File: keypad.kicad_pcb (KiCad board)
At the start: 2 copper layers, 10 parts, among them SW1 SW_Push, SW2 SW_Push, SW3 SW_Push, SW4 SW_Push, SW5 SW_Push, SW6 SW_Push, SW7 SW_Push, SW8 SW_Push, SW9 SW_Push, U1 ESP32-S3-DevKitC-1

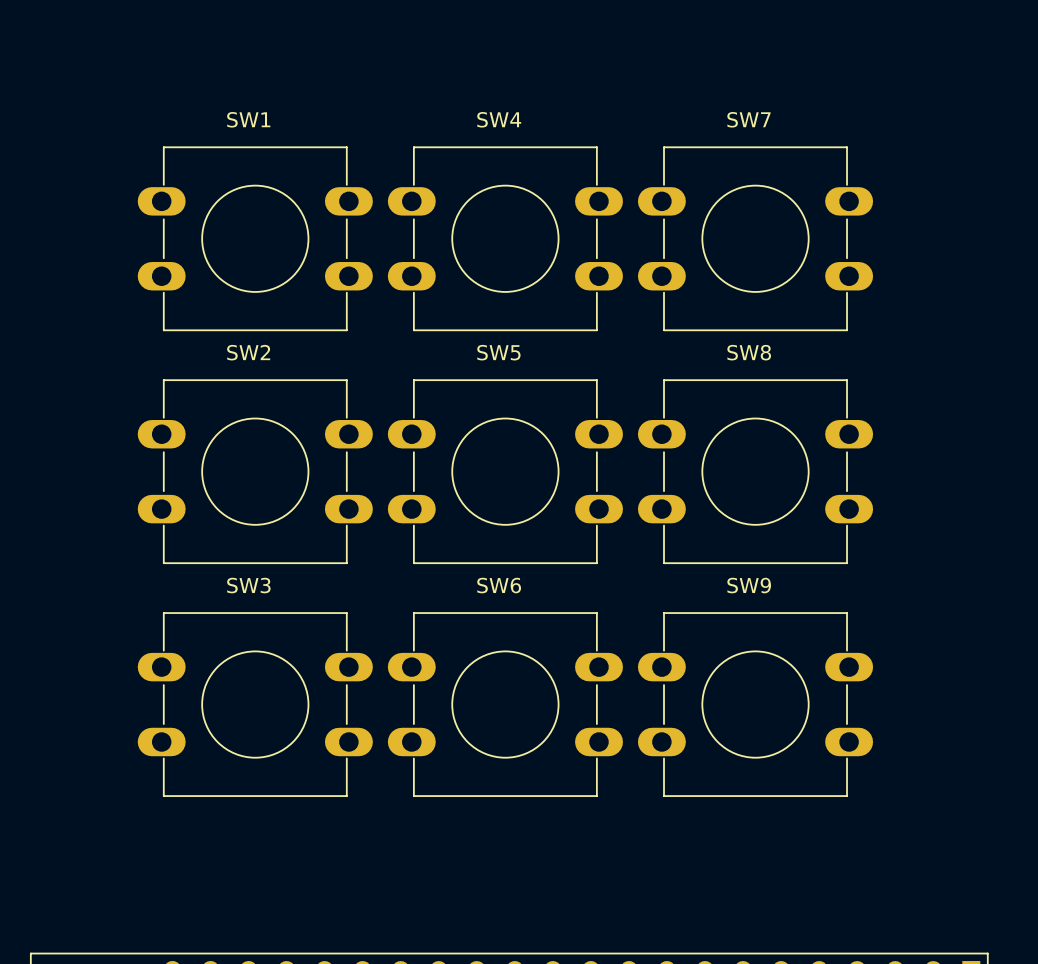
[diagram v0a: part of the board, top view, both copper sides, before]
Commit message: spaced out buttons
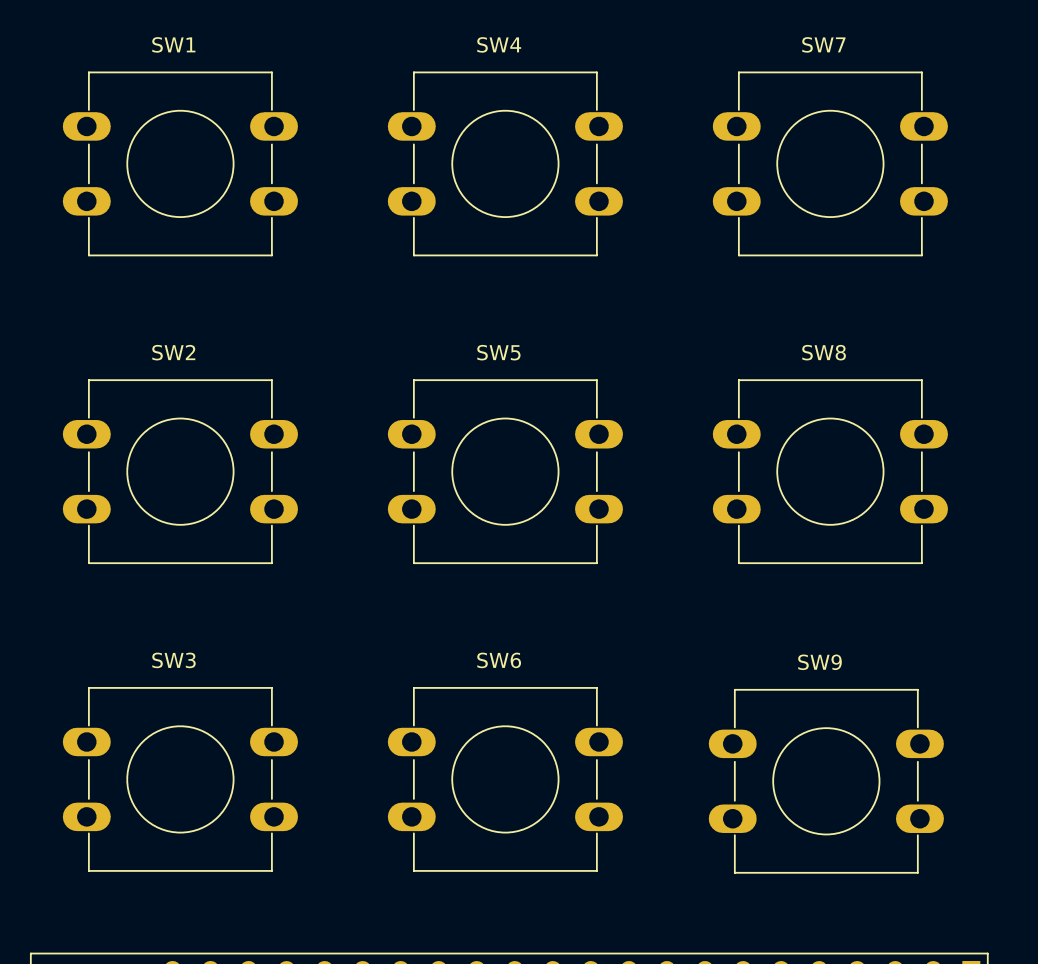
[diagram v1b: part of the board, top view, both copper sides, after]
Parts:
- moved SW1 7.07 mm to (123.6, 66.3)
- moved SW3 7.07 mm to (123.6, 107.4)
- moved SW7 7.07 mm to (167.0, 66.3)
- moved SW9 6.97 mm to (166.8, 107.5)
- moved SW2 5.00 mm to (123.6, 86.8)
- moved SW4 5.00 mm to (145.3, 66.3)
- moved SW6 5.00 mm to (145.3, 107.4)
- moved SW8 5.00 mm to (167.0, 86.8)
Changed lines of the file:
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@@
 	(footprint "Button_Switch_THT:SW_PUSH-12mm"
 		(layer "F.Cu")
-		(at 145.32 102.375)
+		(at 145.32 107.375)
 		(descr "Generic SW PUSH 12mm, e.g https://sten-eswitch-13110800-production.s3.amazonaws.com/system/asset/product_line/data_sheet/143/TL1100.pdf")
 		(tags "tact sw push 12mm")
@@
 	(footprint "Button_Switch_THT:SW_PUSH-12mm"
 		(layer "F.Cu")
-		(at 162.02 71.275)
+		(at 167.02 66.275)
 		(descr "Generic SW PUSH 12mm, e.g https://sten-eswitch-13110800-production.s3.amazonaws.com/system/asset/product_line/data_sheet/143/TL1100.pdf")
 		(tags "tact sw push 12mm")
@@
 	(footprint "Button_Switch_THT:SW_PUSH-12mm"
 		(layer "F.Cu")
-		(at 128.62 86.825)
+		(at 123.62 86.825)
 		(descr "Generic SW PUSH 12mm, e.g https://sten-eswitch-13110800-production.s3.amazonaws.com/system/asset/product_line/data_sheet/143/TL1100.pdf")
 		(tags "tact sw push 12mm")
@@
 	(footprint "Button_Switch_THT:SW_PUSH-12mm"
 		(layer "F.Cu")
-		(at 128.62 71.275)
+		(at 123.62 66.275)
 		(descr "Generic SW PUSH 12mm, e.g https://sten-eswitch-13110800-production.s3.amazonaws.com/system/asset/product_line/data_sheet/143/TL1100.pdf")
 		(tags "tact sw push 12mm")
@@
 	(footprint "Button_Switch_THT:SW_PUSH-12mm"
 		(layer "F.Cu")
-		(at 162.02 102.375)
+		(at 166.75 107.5)
 		(descr "Generic SW PUSH 12mm, e.g https://sten-eswitch-13110800-production.s3.amazonaws.com/system/asset/product_line/data_sheet/143/TL1100.pdf")
 		(tags "tact sw push 12mm")
@@
 	(footprint "Button_Switch_THT:SW_PUSH-12mm"
 		(layer "F.Cu")
-		(at 145.32 71.275)
+		(at 145.32 66.275)
 		(descr "Generic SW PUSH 12mm, e.g https://sten-eswitch-13110800-production.s3.amazonaws.com/system/asset/product_line/data_sheet/143/TL1100.pdf")
 		(tags "tact sw push 12mm")
@@
 	(footprint "Button_Switch_THT:SW_PUSH-12mm"
 		(layer "F.Cu")
-		(at 128.62 102.375)
+		(at 123.62 107.375)
 		(descr "Generic SW PUSH 12mm, e.g https://sten-eswitch-13110800-production.s3.amazonaws.com/system/asset/product_line/data_sheet/143/TL1100.pdf")
 		(tags "tact sw push 12mm")
@@
 	(footprint "Button_Switch_THT:SW_PUSH-12mm"
 		(layer "F.Cu")
-		(at 162.02 86.825)
+		(at 167.02 86.825)
 		(descr "Generic SW PUSH 12mm, e.g https://sten-eswitch-13110800-production.s3.amazonaws.com/system/asset/product_line/data_sheet/143/TL1100.pdf")
 		(tags "tact sw push 12mm")

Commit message: add edge
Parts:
- moved U1 11.1 mm to (172.9, 128.3)
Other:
- board outline added: 67 x 105 mm
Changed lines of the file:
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@@
 		(sheetname "/")
 		(sheetfile "keypad.kicad_sch")
-		(units
-			(unit
-				(name "A")
-				(pins "1" "2")
-			)
-		)
 		(attr through_hole)
 		(duplicate_pad_numbers_are_jumpers no)
@@
 		(sheetname "/")
 		(sheetfile "keypad.kicad_sch")
-		(units
-			(unit
-				(name "A")
-				(pins "1" "2")
-			)
-		)
 		(attr through_hole)
 		(duplicate_pad_numbers_are_jumpers no)
@@
 		(sheetname "/")
 		(sheetfile "keypad.kicad_sch")
-		(units
-			(unit
-				(name "A")
-				(pins "1" "2")
-			)
-		)
 		(attr through_hole)
 		(duplicate_pad_numbers_are_jumpers no)
@@
 		(sheetname "/")
 		(sheetfile "keypad.kicad_sch")
-		(units
-			(unit
-				(name "A")
-				(pins "1" "2")
-			)
-		)
 		(attr through_hole)
 		(duplicate_pad_numbers_are_jumpers no)
@@
 	(footprint "Library:ESP32-S3-DevKitC-1-ish"
 		(layer "F.Cu")
-		(at 182.68 123 -90)
+		(at 172.92344 128.3 -90)
 		(descr "ESP32-S3 general-purpose development board, based on ESP32-S3-WROOM-1 or ESP32-S3-WROOM-1U,It has all the ESP32-S3 pins exposed and is easy to connect and use.")
 		(tags "ESP32-S3")
@@
 		(sheetname "/")
 		(sheetfile "keypad.kicad_sch")
-		(units
-			(unit
-				(name "A")
-				(pins "3" "8" "9" "36" "37" "38" "39" "21" "24" "44" "23" "22" "2" "1"
-					"43" "42" "26" "25" "31" "41" "40" "13" "4" "5" "6" "7" "12" "15" "16"
-					"17" "18" "19" "20" "10" "11" "27" "32" "33" "34" "35" "30" "14" "28"
-					"29"
-				)
-			)
-		)
 		(attr through_hole)
 		(duplicate_pad_numbers_are_jumpers no)
 		(fp_line
-			(start -1.5 62.79728)
-			(end 26.8986 62.79728)
+			(start -1.5 54.86)
+			(end 26.8986 54.86)
 			(stroke
 				(width 0.12)
@@
 		)
 		(fp_line
-			(start 26.899999 62.79728)
+			(start 26.899999 54.86)
 			(end 26.9 -1.1)
 			(stroke
@@
 		(fp_line
 			(start -1.499999 -1.1)
-			(end -1.5 62.79728)
+			(end -1.5 54.86)
 			(stroke
 				(width 0.12)
@@
 		)
 		(fp_line
-			(start -1.25 62.54728)
+			(start -1.25 54.61)
 			(end -1.25 -0.85)
 			(stroke
@@
 		)
 		(fp_line
-			(start 26.6446 62.54728)
-			(end -1.25 62.54728)
+			(start 26.6446 54.61)
+			(end -1.25 54.61)
 			(stroke
 				(width 0.05)
@@
 		(fp_line
 			(start 26.65 -0.85)
-			(end 26.65 62.54728)
+			(end 26.65 54.61)
 			(stroke
 				(width 0.05)
@@
 		(sheetname "/")
 		(sheetfile "keypad.kicad_sch")
-		(units
-			(unit
-				(name "A")
-				(pins "1" "2")
-			)
-		)
 		(attr through_hole)
 		(duplicate_pad_numbers_are_jumpers no)
@@
 		(sheetname "/")
 		(sheetfile "keypad.kicad_sch")
-		(units
-			(unit
-				(name "A")
-				(pins "1" "2")
-			)
-		)
 		(attr through_hole)
 		(duplicate_pad_numbers_are_jumpers no)
@@
 		(sheetname "/")
 		(sheetfile "keypad.kicad_sch")
-		(units
-			(unit
-				(name "A")
-				(pins "1" "2")
-			)
-		)
 		(attr through_hole)
 		(duplicate_pad_numbers_are_jumpers no)
@@
 		(sheetname "/")
 		(sheetfile "keypad.kicad_sch")
-		(units
-			(unit
-				(name "A")
-				(pins "1" "2")
-			)
-		)
 		(attr through_hole)
 		(duplicate_pad_numbers_are_jumpers no)
@@
 		(sheetname "/")
 		(sheetfile "keypad.kicad_sch")
-		(units
-			(unit
-				(name "A")
-				(pins "1" "2")
-			)
-		)
 		(attr through_hole)
 		(duplicate_pad_numbers_are_jumpers no)
@@
 		)
 	)
+	(gr_line
+		(start 118 61)
+		(end 118 160)
+		(stroke
+			(width 0.05)
+			(type default)
+		)
+		(layer "Edge.Cuts")
+	)
+	(gr_arc
+		(start 118 61)
+		(mid 118.87868 58.87868)
+		(end 121 58)
+		(stroke
+			(width 0.05)
+			(type default)
+		)
+		(layer "Edge.Cuts")
+	)
+	(gr_arc
+		(start 121 163)
+		(mid 118.87868 162.12132)
+		(end 118 160)
+		(stroke
+			(width 0.05)
+			(type default)
+		)
+		(layer "Edge.Cuts")
+	)
+	(gr_line
+		(start 121 163)
+		(end 182 163)
+		(stroke
+			(width 0.05)
+			(type default)
+		)
+		(layer "Edge.Cuts")
+	)
+	(gr_line
+		(start 182 58)
+		(end 121 58)
+		(stroke
+			(width 0.05)
+			(type default)
+		)
+		(layer "Edge.Cuts")
+	)
+	(gr_arc
+		(start 182 58)
+		(mid 184.12132 58.87868)
+		(end 185 61)
+		(stroke
+			(width 0.05)
+			(type default)
+		)
+		(layer "Edge.Cuts")
+	)
+	(gr_arc
+		(start 185 160)
+		(mid 184.12132 162.12132)
+		(end 182 163)
+		(stroke
+			(width 0.05)
+			(type default)
+		)
+		(layer "Edge.Cuts")
+	)
+	(gr_line
+		(start 185 160)
+		(end 185 61)
+		(stroke
+			(width 0.05)
+			(type default)
+		)
+		(layer "Edge.Cuts")
+	)
 	(embedded_fonts no)

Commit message: move connections
I moved all the connections so that they make more sense on the pbc.
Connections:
- SW1 pad 1: Net-(U1-GPIO1/ADC1_CH0) -> unconnected-(SW1-Pad1)
- SW1 pad 2: GND -> Net-(U1-GPIO12/ADC2_CH1)
- SW2 pad 1: Net-(U1-GPIO2/ADC1_CH1) -> unconnected-(SW2-Pad1)
- SW2 pad 2: GND -> Net-(U1-GPIO11/ADC2_CH0)
- SW3 pad 1: Net-(U1-GPIO4/ADC1_CH3) -> GND
- SW3 pad 2: GND -> Net-(U1-GPIO10/ADC1_CH9)
- SW4 pad 1: Net-(U1-GPIO5/ADC1_CH4) -> unconnected-(SW4-Pad1)
- SW4 pad 2: GND -> Net-(U1-GPIO9/ADC1_CH8)
- SW5 pad 1: Net-(U1-GPIO6/ADC1_CH5) -> unconnected-(SW5-Pad1)
- SW5 pad 2: GND -> Net-(U1-GPIO8/ADC1_CH7)
- SW6 pad 1: Net-(U1-GPIO7/ADC1_CH6) -> GND
- SW6 pad 2: GND -> Net-(U1-GPIO7/ADC1_CH6)
- SW7 pad 1: Net-(U1-GPIO8/ADC1_CH7) -> unconnected-(SW7-Pad1)
- SW7 pad 2: GND -> Net-(U1-GPIO6/ADC1_CH5)
- SW8 pad 1: Net-(U1-GPIO9/ADC1_CH8) -> unconnected-(SW8-Pad1)
- SW8 pad 2: GND -> Net-(U1-GPIO5/ADC1_CH4)
- SW9 pad 1: Net-(U1-GPIO10/ADC1_CH9) -> GND
- SW9 pad 2: GND -> Net-(U1-GPIO4/ADC1_CH3)
- U1 pad 17: unconnected-(U1-GPIO11/ADC2_CH0-Pad17) -> Net-(U1-GPIO11/ADC2_CH0)
- U1 pad 18: unconnected-(U1-GPIO12/ADC2_CH1-Pad18) -> Net-(U1-GPIO12/ADC2_CH1)
- U1 pad 40: Net-(U1-GPIO2/ADC1_CH1) -> unconnected-(U1-GPIO2/ADC1_CH1-Pad40)
- U1 pad 41: Net-(U1-GPIO1/ADC1_CH0) -> unconnected-(U1-GPIO1/ADC1_CH0-Pad41)
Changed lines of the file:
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@@
 		(sheetname "/")
 		(sheetfile "keypad.kicad_sch")
+		(units
+			(unit
+				(name "A")
+				(pins "1" "2")
+			)
+		)
 		(attr through_hole)
 		(duplicate_pad_numbers_are_jumpers no)
@@
 			(layers "*.Cu" "*.Mask")
 			(remove_unused_layers no)
-			(net "Net-(U1-GPIO7{slash}ADC1_CH6)")
+			(net "GND")
 			(pinfunction "1_1")
 			(pintype "passive")
@@
 			(layers "*.Cu" "*.Mask")
 			(remove_unused_layers no)
-			(net "Net-(U1-GPIO7{slash}ADC1_CH6)")
+			(net "GND")
 			(pinfunction "1_1")
 			(pintype "passive")
@@
 			(layers "*.Cu" "*.Mask")
 			(remove_unused_layers no)
-			(net "GND")
+			(net "Net-(U1-GPIO7{slash}ADC1_CH6)")
 			(pinfunction "2_2")
 			(pintype "passive")
@@
 			(layers "*.Cu" "*.Mask")
 			(remove_unused_layers no)
-			(net "GND")
+			(net "Net-(U1-GPIO7{slash}ADC1_CH6)")
 			(pinfunction "2_2")
 			(pintype "passive")
@@
 		(sheetname "/")
 		(sheetfile "keypad.kicad_sch")
+		(units
+			(unit
+				(name "A")
+				(pins "1" "2")
+			)
+		)
 		(attr through_hole)
 		(duplicate_pad_numbers_are_jumpers no)
@@
 			(layers "*.Cu" "*.Mask")
 			(remove_unused_layers no)
-			(net "Net-(U1-GPIO8{slash}ADC1_CH7)")
+			(net "unconnected-(SW7-Pad1)")
 			(pinfunction "1_1")
 			(pintype "passive")
@@
 			(layers "*.Cu" "*.Mask")
 			(remove_unused_layers no)
-			(net "Net-(U1-GPIO8{slash}ADC1_CH7)")
+			(net "unconnected-(SW7-Pad1)")
 			(pinfunction "1_1")
 			(pintype "passive")
@@
 			(layers "*.Cu" "*.Mask")
 			(remove_unused_layers no)
-			(net "GND")
+			(net "Net-(U1-GPIO6{slash}ADC1_CH5)")
 			(pinfunction "2_2")
 			(pintype "passive")
@@
 			(layers "*.Cu" "*.Mask")
 			(remove_unused_layers no)
-			(net "GND")
+			(net "Net-(U1-GPIO6{slash}ADC1_CH5)")
 			(pinfunction "2_2")
 			(pintype "passive")
@@
 		(sheetname "/")
 		(sheetfile "keypad.kicad_sch")
+		(units
+			(unit
+				(name "A")
+				(pins "1" "2")
+			)
+		)
 		(attr through_hole)
 		(duplicate_pad_numbers_are_jumpers no)
@@
 			(layers "*.Cu" "*.Mask")
 			(remove_unused_layers no)
-			(net "Net-(U1-GPIO2{slash}ADC1_CH1)")
+			(net "unconnected-(SW2-Pad1)")
 			(pinfunction "1_1")
 			(pintype "passive")
@@
 			(layers "*.Cu" "*.Mask")
 			(remove_unused_layers no)
-			(net "Net-(U1-GPIO2{slash}ADC1_CH1)")
+			(net "unconnected-(SW2-Pad1)")
 			(pinfunction "1_1")
 			(pintype "passive")
@@
 			(layers "*.Cu" "*.Mask")
 			(remove_unused_layers no)
-			(net "GND")
+			(net "Net-(U1-GPIO11{slash}ADC2_CH0)")
 			(pinfunction "2_2")
 			(pintype "passive")
@@
 			(layers "*.Cu" "*.Mask")
 			(remove_unused_layers no)
-			(net "GND")
+			(net "Net-(U1-GPIO11{slash}ADC2_CH0)")
 			(pinfunction "2_2")
 			(pintype "passive")
@@
 		(sheetname "/")
 		(sheetfile "keypad.kicad_sch")
+		(units
+			(unit
+				(name "A")
+				(pins "1" "2")
+			)
+		)
 		(attr through_hole)
 		(duplicate_pad_numbers_are_jumpers no)
@@
 			(layers "*.Cu" "*.Mask")
 			(remove_unused_layers no)
-			(net "Net-(U1-GPIO6{slash}ADC1_CH5)")
+			(net "unconnected-(SW5-Pad1)")
 			(pinfunction "1_1")
 			(pintype "passive")
@@
 			(layers "*.Cu" "*.Mask")
 			(remove_unused_layers no)
-			(net "Net-(U1-GPIO6{slash}ADC1_CH5)")
+			(net "unconnected-(SW5-Pad1)")
 			(pinfunction "1_1")
 			(pintype "passive")
@@
 			(layers "*.Cu" "*.Mask")
 			(remove_unused_layers no)
-			(net "GND")
+			(net "Net-(U1-GPIO8{slash}ADC1_CH7)")
 			(pinfunction "2_2")
 			(pintype "passive")
@@
 			(layers "*.Cu" "*.Mask")
 			(remove_unused_layers no)
-			(net "GND")
+			(net "Net-(U1-GPIO8{slash}ADC1_CH7)")
 			(pinfunction "2_2")
 			(pintype "passive")
@@
 		(sheetname "/")
 		(sheetfile "keypad.kicad_sch")
+		(units
+			(unit
+				(name "A")
+				(pins "3" "8" "9" "36" "37" "38" "39" "21" "24" "44" "23" "22" "2" "1"
+					"43" "42" "26" "25" "31" "41" "40" "13" "4" "5" "6" "7" "12" "15" "16"
+					"17" "18" "19" "20" "10" "11" "27" "32" "33" "34" "35" "30" "14" "28"
+					"29"
+				)
+			)
+		)
 		(attr through_hole)
 		(duplicate_pad_numbers_are_jumpers no)
@@
 			(layers "*.Cu" "*.Mask")
 			(remove_unused_layers no)
-			(net "unconnected-(U1-GPIO11{slash}ADC2_CH0-Pad17)")
+			(net "Net-(U1-GPIO11{slash}ADC2_CH0)")
 			(pinfunction "GPIO11/ADC2_CH0_17")
 			(pintype "bidirectional")
@@
 			(layers "*.Cu" "*.Mask")
 			(remove_unused_layers no)
-			(net "unconnected-(U1-GPIO12{slash}ADC2_CH1-Pad18)")
+			(net "Net-(U1-GPIO12{slash}ADC2_CH1)")
 			(pinfunction "GPIO12/ADC2_CH1_18")
 			(pintype "bidirectional")
@@
 			(layers "*.Cu" "*.Mask")
 			(remove_unused_layers no)
-			(net "Net-(U1-GPIO2{slash}ADC1_CH1)")
+			(net "unconnected-(U1-GPIO2{slash}ADC1_CH1-Pad40)")
 			(pinfunction "GPIO2/ADC1_CH1_40")
 			(pintype "bidirectional")
@@
 			(layers "*.Cu" "*.Mask")
 			(remove_unused_layers no)
-			(net "Net-(U1-GPIO1{slash}ADC1_CH0)")
+			(net "unconnected-(U1-GPIO1{slash}ADC1_CH0-Pad41)")
 			(pinfunction "GPIO1/ADC1_CH0_41")
 			(pintype "bidirectional")
@@
 		(sheetname "/")
 		(sheetfile "keypad.kicad_sch")
+		(units
+			(unit
+				(name "A")
+				(pins "1" "2")
+			)
+		)
 		(attr through_hole)
 		(duplicate_pad_numbers_are_jumpers no)
@@
 			(layers "*.Cu" "*.Mask")
 			(remove_unused_layers no)
-			(net "Net-(U1-GPIO1{slash}ADC1_CH0)")
+			(net "unconnected-(SW1-Pad1)")
 			(pinfunction "1_1")
 			(pintype "passive")
@@
 			(layers "*.Cu" "*.Mask")
 			(remove_unused_layers no)
-			(net "Net-(U1-GPIO1{slash}ADC1_CH0)")
+			(net "unconnected-(SW1-Pad1)")
 			(pinfunction "1_1")
 			(pintype "passive")
@@
 			(layers "*.Cu" "*.Mask")
 			(remove_unused_layers no)
-			(net "GND")
+			(net "Net-(U1-GPIO12{slash}ADC2_CH1)")
 			(pinfunction "2_2")
 			(pintype "passive")
@@
 			(layers "*.Cu" "*.Mask")
 			(remove_unused_layers no)
-			(net "GND")
+			(net "Net-(U1-GPIO12{slash}ADC2_CH1)")
 			(pinfunction "2_2")
 			(pintype "passive")
@@
 		(sheetname "/")
 		(sheetfile "keypad.kicad_sch")
+		(units
+			(unit
+				(name "A")
+				(pins "1" "2")
+			)
+		)
 		(attr through_hole)
 		(duplicate_pad_numbers_are_jumpers no)
@@
 			(layers "*.Cu" "*.Mask")
 			(remove_unused_layers no)
-			(net "Net-(U1-GPIO10{slash}ADC1_CH9)")
+			(net "GND")
 			(pinfunction "1_1")
 			(pintype "passive")
@@
 			(layers "*.Cu" "*.Mask")
 			(remove_unused_layers no)
-			(net "Net-(U1-GPIO10{slash}ADC1_CH9)")
+			(net "GND")
 			(pinfunction "1_1")
 			(pintype "passive")
@@
 			(layers "*.Cu" "*.Mask")
 			(remove_unused_layers no)
-			(net "GND")
+			(net "Net-(U1-GPIO4{slash}ADC1_CH3)")
 			(pinfunction "2_2")
 			(pintype "passive")
@@
 			(layers "*.Cu" "*.Mask")
 			(remove_unused_layers no)
-			(net "GND")
+			(net "Net-(U1-GPIO4{slash}ADC1_CH3)")
 			(pinfunction "2_2")
 			(pintype "passive")
@@
 		(sheetname "/")
 		(sheetfile "keypad.kicad_sch")
+		(units
+			(unit
+				(name "A")
+				(pins "1" "2")
+			)
+		)
 		(attr through_hole)
 		(duplicate_pad_numbers_are_jumpers no)
@@
 			(layers "*.Cu" "*.Mask")
 			(remove_unused_layers no)
-			(net "Net-(U1-GPIO5{slash}ADC1_CH4)")
+			(net "unconnected-(SW4-Pad1)")
 			(pinfunction "1_1")
 			(pintype "passive")
@@
 			(layers "*.Cu" "*.Mask")
 			(remove_unused_layers no)
-			(net "Net-(U1-GPIO5{slash}ADC1_CH4)")
+			(net "unconnected-(SW4-Pad1)")
 			(pinfunction "1_1")
 			(pintype "passive")
@@
 			(layers "*.Cu" "*.Mask")
 			(remove_unused_layers no)
-			(net "GND")
+			(net "Net-(U1-GPIO9{slash}ADC1_CH8)")
 			(pinfunction "2_2")
 			(pintype "passive")
@@
 			(layers "*.Cu" "*.Mask")
 			(remove_unused_layers no)
-			(net "GND")
+			(net "Net-(U1-GPIO9{slash}ADC1_CH8)")
 			(pinfunction "2_2")
 			(pintype "passive")
@@
 		(sheetname "/")
 		(sheetfile "keypad.kicad_sch")
+		(units
+			(unit
+				(name "A")
+				(pins "1" "2")
+			)
+		)
 		(attr through_hole)
 		(duplicate_pad_numbers_are_jumpers no)
@@
 			(layers "*.Cu" "*.Mask")
 			(remove_unused_layers no)
-			(net "Net-(U1-GPIO4{slash}ADC1_CH3)")
+			(net "GND")
 			(pinfunction "1_1")
 			(pintype "passive")
@@
 			(layers "*.Cu" "*.Mask")
 			(remove_unused_layers no)
-			(net "Net-(U1-GPIO4{slash}ADC1_CH3)")
+			(net "GND")
 			(pinfunction "1_1")
 			(pintype "passive")
@@
 			(layers "*.Cu" "*.Mask")
 			(remove_unused_layers no)
-			(net "GND")
+			(net "Net-(U1-GPIO10{slash}ADC1_CH9)")
 			(pinfunction "2_2")
 			(pintype "passive")
@@
 			(layers "*.Cu" "*.Mask")
 			(remove_unused_layers no)
-			(net "GND")
+			(net "Net-(U1-GPIO10{slash}ADC1_CH9)")
 			(pinfunction "2_2")
 			(pintype "passive")
@@
 		(sheetname "/")
 		(sheetfile "keypad.kicad_sch")
+		(units
+			(unit
+				(name "A")
+				(pins "1" "2")
+			)
+		)
 		(attr through_hole)
 		(duplicate_pad_numbers_are_jumpers no)
@@
 			(layers "*.Cu" "*.Mask")
 			(remove_unused_layers no)
-			(net "Net-(U1-GPIO9{slash}ADC1_CH8)")
+			(net "unconnected-(SW8-Pad1)")
 			(pinfunction "1_1")
 			(pintype "passive")
@@
 			(layers "*.Cu" "*.Mask")
 			(remove_unused_layers no)
-			(net "Net-(U1-GPIO9{slash}ADC1_CH8)")
+			(net "unconnected-(SW8-Pad1)")
 			(pinfunction "1_1")
 			(pintype "passive")
@@
 			(layers "*.Cu" "*.Mask")
 			(remove_unused_layers no)
-			(net "GND")
+			(net "Net-(U1-GPIO5{slash}ADC1_CH4)")
 			(pinfunction "2_2")
 			(pintype "passive")
@@
 			(layers "*.Cu" "*.Mask")
 			(remove_unused_layers no)
-			(net "GND")
+			(net "Net-(U1-GPIO5{slash}ADC1_CH4)")
 			(pinfunction "2_2")
 			(pintype "passive")

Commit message: route board
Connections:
- SW1 pad 1: unconnected-(SW1-Pad1) -> GND
- SW2 pad 1: unconnected-(SW2-Pad1) -> GND
- SW4 pad 1: unconnected-(SW4-Pad1) -> GND
- SW5 pad 1: unconnected-(SW5-Pad1) -> GND
- SW7 pad 1: unconnected-(SW7-Pad1) -> GND
- SW8 pad 1: unconnected-(SW8-Pad1) -> GND
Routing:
- net GND: track 0.00 -> 263.9 mm
- net Net-(U1-GPIO9/ADC1_CH8): track 0.00 -> 60.3 mm
- net Net-(U1-GPIO6/ADC1_CH5): track 0.00 -> 59.8 mm
- net Net-(U1-GPIO12/ADC2_CH1): track 0.00 -> 59.7 mm
- net Net-(U1-GPIO5/ADC1_CH4): track 0.00 -> 38.2 mm
- net Net-(U1-GPIO11/ADC2_CH0): track 0.00 -> 38.1 mm
- net Net-(U1-GPIO8/ADC1_CH7): track 0.00 -> 37.9 mm
- net Net-(U1-GPIO10/ADC1_CH9): track 0.00 -> 16.5 mm
- net Net-(U1-GPIO4/ADC1_CH3): track 0.00 -> 16.4 mm
- net Net-(U1-GPIO7/ADC1_CH6): track 0.00 -> 16.0 mm
